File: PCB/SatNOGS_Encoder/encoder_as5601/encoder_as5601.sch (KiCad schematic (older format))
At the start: 6 parts, among them P1 CONN_02X05, U1 AS5601

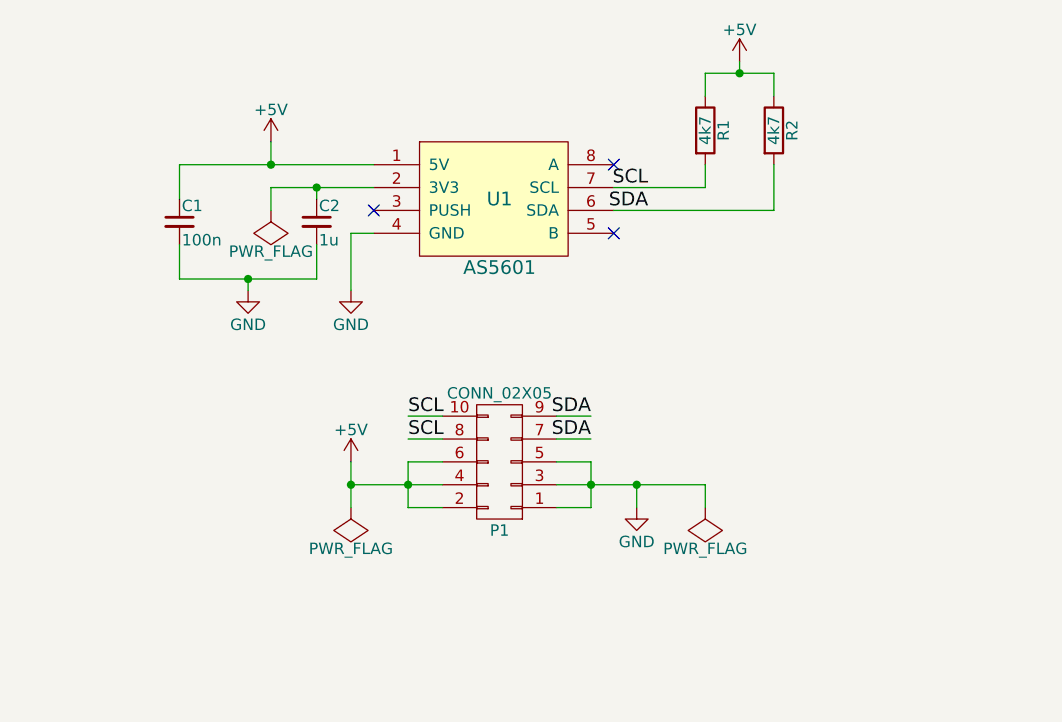
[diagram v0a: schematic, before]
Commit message: Add reverse current protection and update pcb.
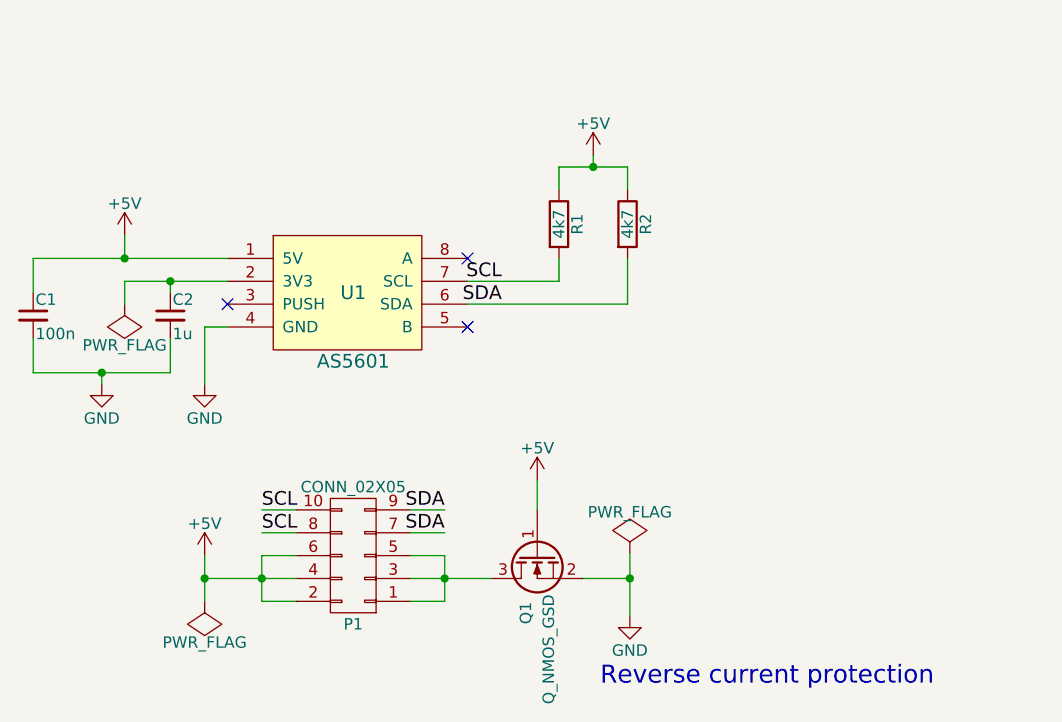
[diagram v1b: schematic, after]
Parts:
- added Q1: Q_NMOS_GSD, TO_SOT_Packages_SMD:SOT-23_Handsoldering, symbol Q_NMOS_GSD
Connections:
- net +5V: now also Q1.1 (G)
- net GND: now also Q1.2 (S); no longer P1.1 (P1), P1.3 (P3), P1.5 (P5)
- new net: P1.1 (P1), P1.3 (P3), P1.5 (P5), Q1.3 (D)
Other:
- note added: "Reverse current protection"
- moved on the sheet: C1, C2, P1, R1, R2, U1

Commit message: Update BOM's.
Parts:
- Q1: Notes (none) -> -
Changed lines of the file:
@@
 F 5 "SI2312CDS-T1-GE3" H 6315 4610 60  0001 C CNN "Manufacturer"
 F 6 "SOT-23-3" H 6315 4610 60  0001 C CNN "Package"
-F 7 "0.398" H 6315 4610 60  0001 C CNN "Price"
+F 7 "-" H 6315 4610 60  0001 C CNN "Notes"
+F 8 "0.398" H 6315 4610 60  0001 C CNN "Price"
 	1    6315 4610
 	0    -1   1    0

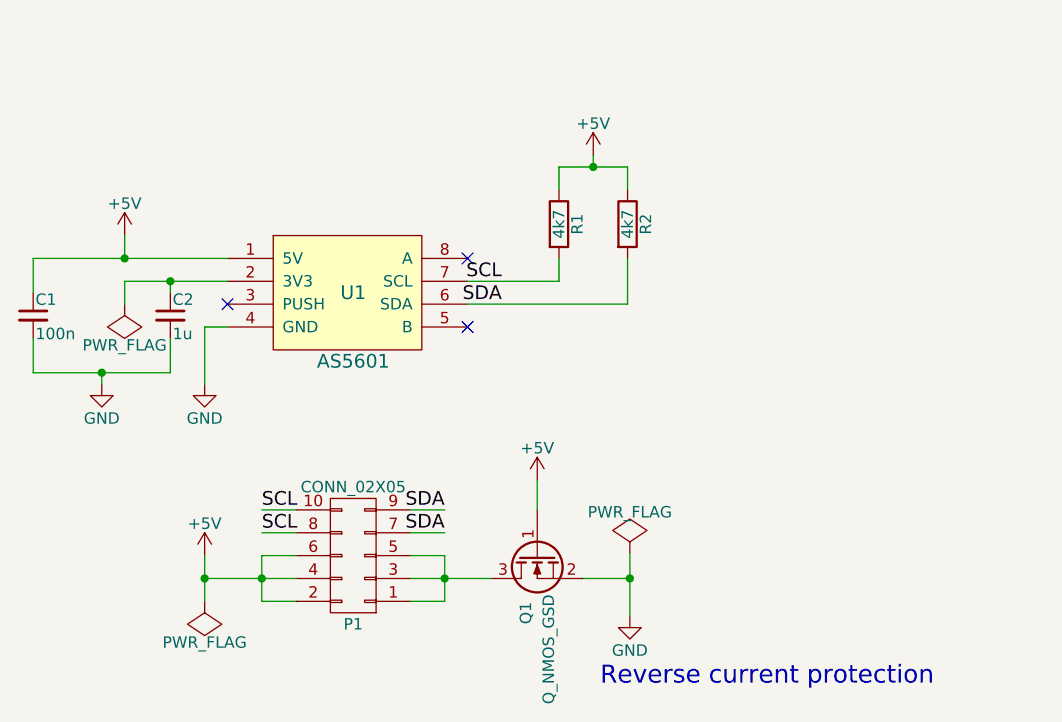
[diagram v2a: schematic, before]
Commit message: Update pcb to mount in cas.
Add mount holes.
Rearraange parts in order to place the AS5601 in the middle of PCB.
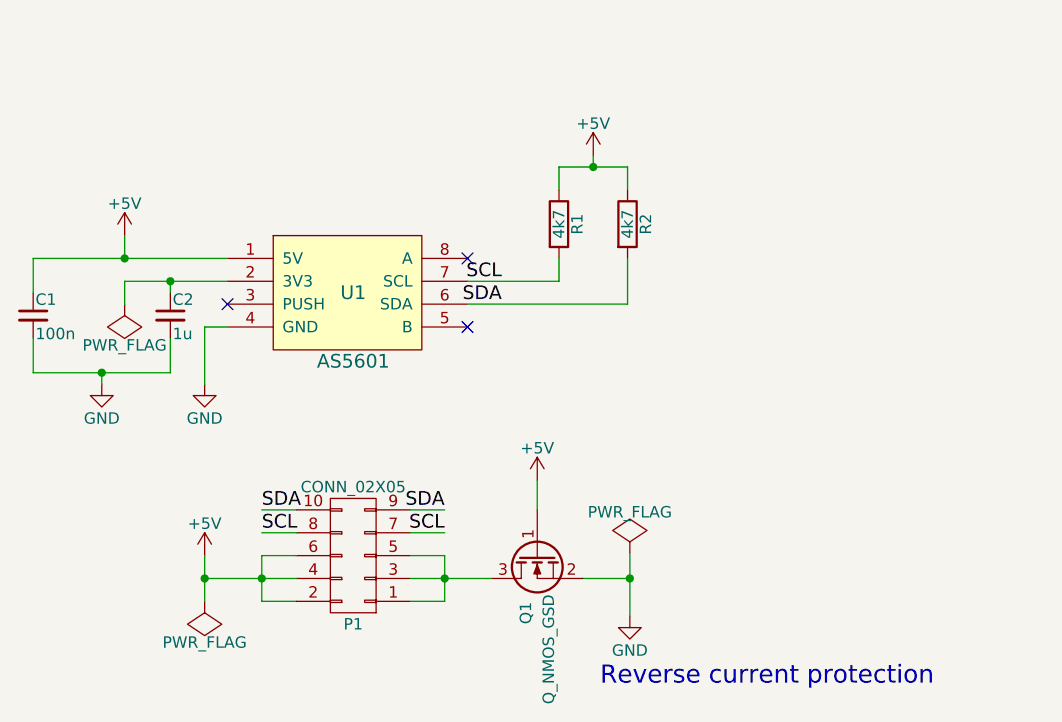
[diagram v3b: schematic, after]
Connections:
- net SCL: now also P1.7 (P7); no longer P1.10 (P10)
- net SDA: now also P1.10 (P10); no longer P1.7 (P7)
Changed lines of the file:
@@
 	-1   0    0    1
 $EndComp
-Text Label 5110 4410 0    60   ~ 0
+Text Label 5110 4510 0    60   ~ 0
 SCL
-Text Label 5910 4510 2    60   ~ 0
+Text Label 5910 4410 2    60   ~ 0
 SDA
 $Comp
@@
 $EndComp
 Connection ~ 4860 4710
-Text Label 5910 4410 2    60   ~ 0
+Text Label 5110 4410 0    60   ~ 0
 SDA
-Text Label 5110 4510 0    60   ~ 0
+Text Label 5910 4510 2    60   ~ 0
 SCL
 $Comp
